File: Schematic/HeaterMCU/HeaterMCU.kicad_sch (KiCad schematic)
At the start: 59 parts, among them J301 To PSU Board, J302 Heater Control, J303 High voltage warning, J304 Firmware, SW301 RESET, U301 Display_IPS_1.3_SPI, U302 ATMEGA328P-AU, U303 TLP185, U304 INA219AIDCNR, U305 TLP185, U306 TPS54302, Y301 8MHz

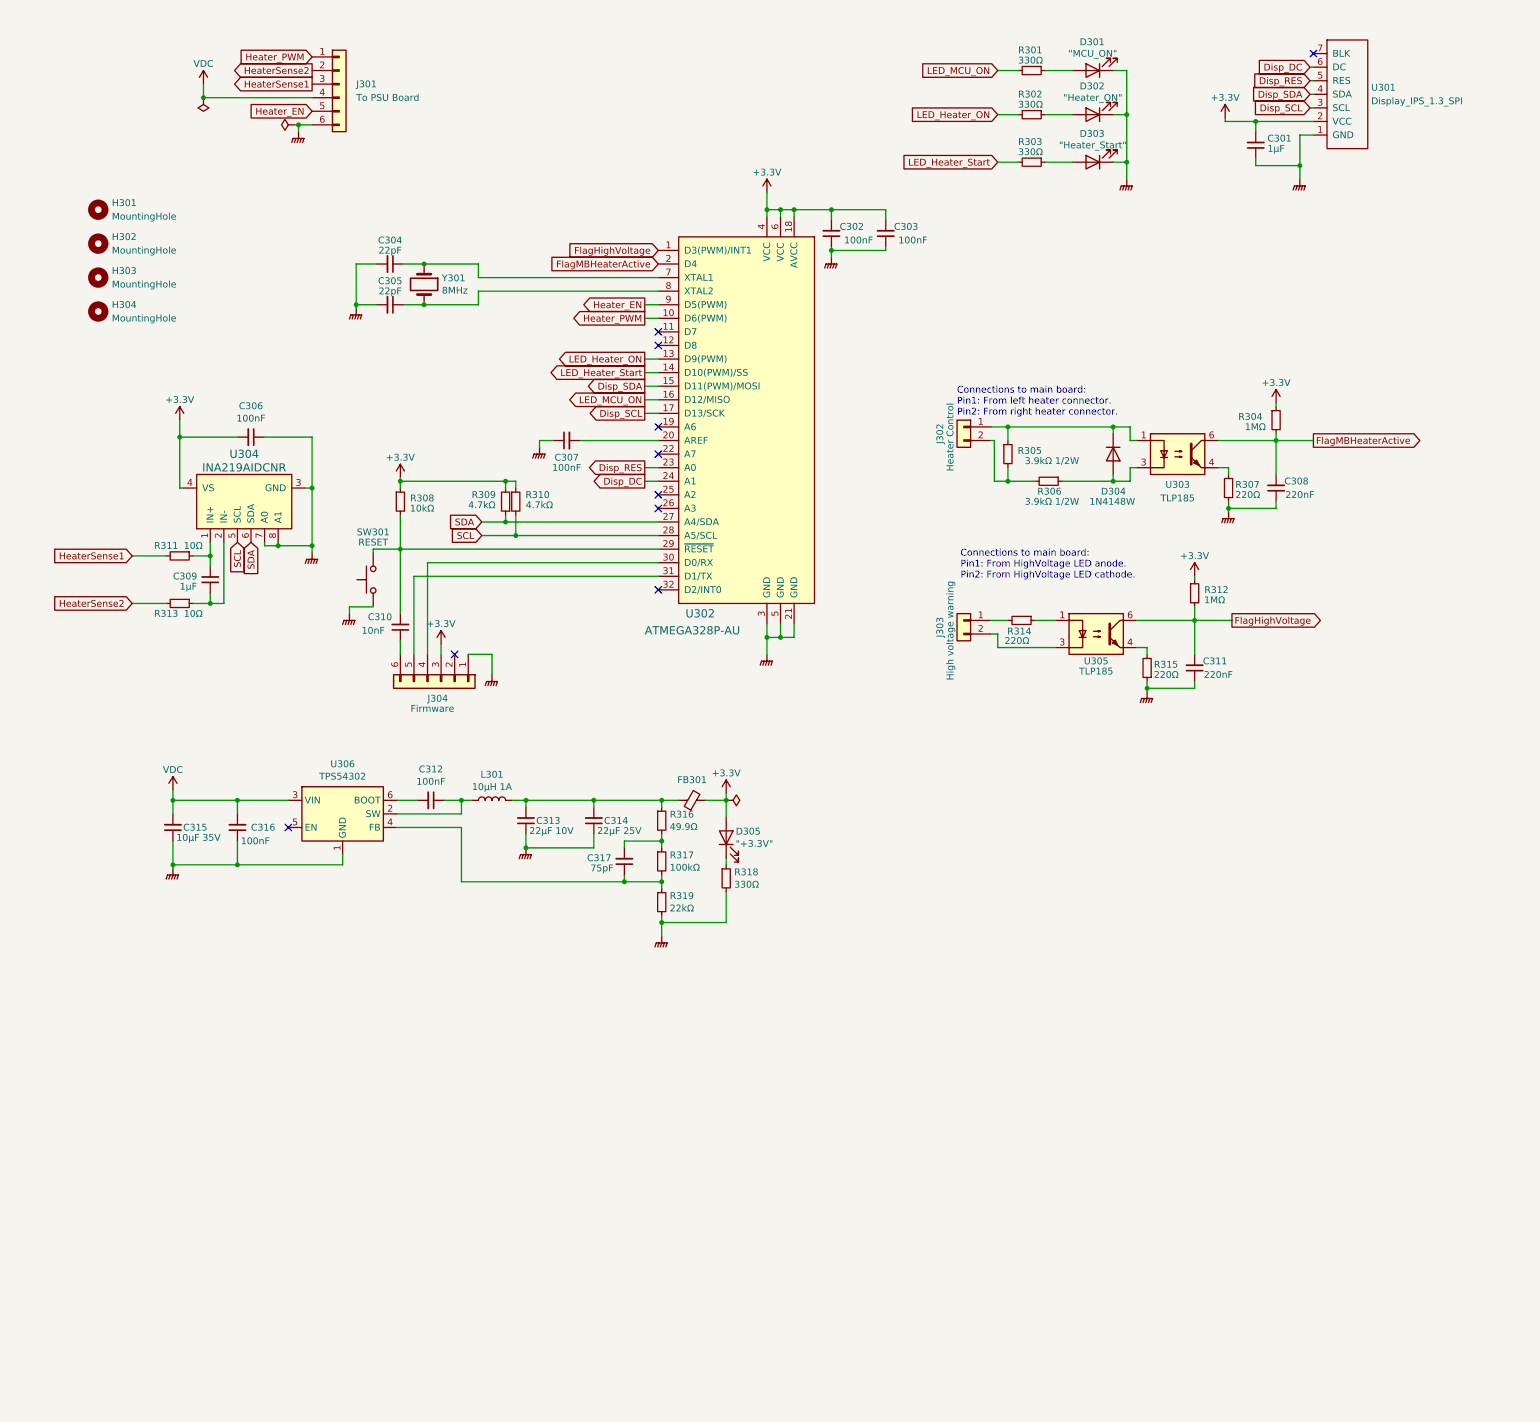
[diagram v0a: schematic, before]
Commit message: New PSU based on XL4005
Added current limiter
Added interface to uTracer PIC
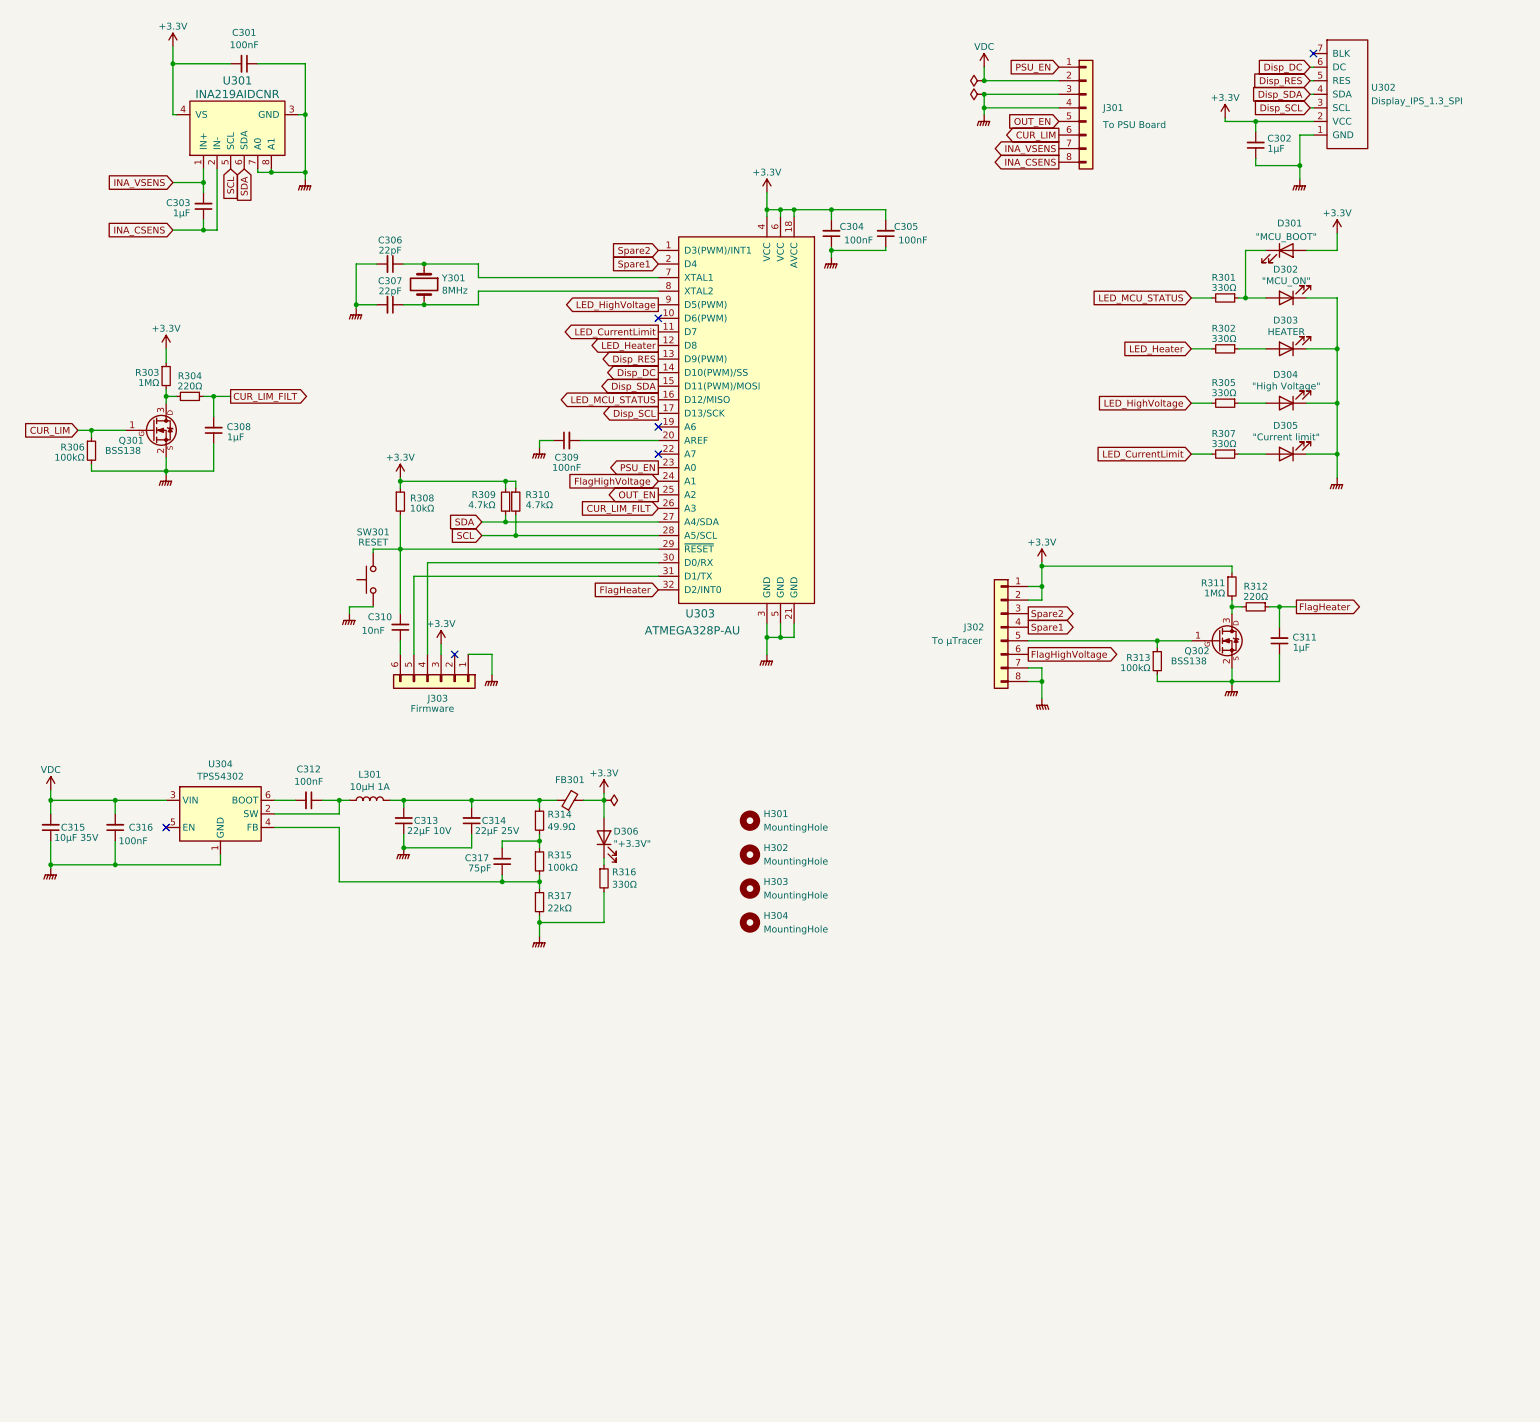
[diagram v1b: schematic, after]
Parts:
- removed D304: 1N4148W, Diode_SMD:D_SOD-123, symbol Diode:1N4148W
- removed J301: To PSU Board, Connector_PinSocket_2.54mm:PinSocket_1x06_P2.54mm_Vertical, symbol Connector_Generic:Conn_01x06
- removed J302: Heater Control, Connector_PinSocket_2.54mm:PinSocket_1x02_P2.54mm_Horizontal, symbol Connector_Generic:Conn_01x02
- removed J303: High voltage warning, Connector_PinSocket_2.54mm:PinSocket_1x02_P2.54mm_Horizontal, symbol Connector_Generic:Conn_01x02
- removed R305: 3.9kΩ 1/2W, Resistor_SMD:R_1210_3225Metric_Pad1.30x2.65mm_HandSolder, symbol Device:R_Small
- removed R314, R315: 220Ω, Resistor_SMD:R_0603_1608Metric_Pad0.98x0.95mm_HandSolder, symbol Device:R_Small
- removed U303, U305: TLP185, Package_SO:SOIC-4_4.55x3.7mm_P2.54mm, symbol Isolator:TLP185
- added D301: "MCU_BOOT", LED_SMD:LED_0603_1608Metric_Pad1.05x0.95mm_HandSolder, symbol Device:LED
- added D305: "Current limit", LED_SMD:LED_0603_1608Metric_Pad1.05x0.95mm_HandSolder, symbol Device:LED
- added J301: To PSU Board, Connector_PinHeader_2.54mm:PinHeader_1x08_P2.54mm_Vertical, symbol Connector_Generic:Conn_01x08
- added J302: To µTracer, myDevices:0527450897, symbol Connector_Generic:Conn_01x08
- added Q301, Q302: BSS138, Package_TO_SOT_SMD:SOT-23, symbol myDevices:BSS138
- added R303: 1MΩ, Resistor_SMD:R_0603_1608Metric_Pad0.98x0.95mm_HandSolder, symbol Device:R_Small
- C308, C311: value 220nF -> 1µF
- D303: renamed from D302; value "Heater_ON" -> HEATER
- D304: renamed from D303; value "Heater_Start" -> "High Voltage"
- R304, R312: value 1MΩ -> 220Ω
- R306: value 3.9kΩ 1/2W -> 100kΩ; footprint Resistor_SMD:R_1210_3225Metric_Pad1.30x2.65mm_HandSolder -> Resistor_SMD:R_0603_1608Metric_Pad0.98x0.95mm_HandSolder
- R307: value 220Ω -> 330Ω
- R311: value 10Ω -> 1MΩ
- R313: value 10Ω -> 100kΩ
- renumbered C306 to C301, C301 to C302, C309 to C303, C302 to C304, C303 to C305, C304 to C306, C305 to C307, C307 to C309, D301 to D302, D305 to D306, J304 to J303, R303 to R305, R316 to R314, R317 to R315, R318 to R316, R319 to R317, U304 to U301, U301 to U302, U302 to U303, U306 to U304
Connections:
- net HeaterSense2 is gone; now on net GNDPWR: R313.2
- net +3V3: now also R311.1, D301.2 (A), J302.1 (Pin_1), J302.2 (Pin_2), R303.1; no longer R304.1, R312.1
- net Disp_DC: now also U303.14 (D10(PWM)/SS); no longer U303.24 (A1)
- net Disp_RES: now also U303.13 (D9(PWM)); no longer U303.23 (A0)
- net FlagHighVoltage: now also U303.24 (A1), J302.6 (Pin_6); no longer C311.2, R312.2, U303.1 (D3(PWM)/INT1)
- net GNDPWR: now also R306.2, D305.1 (K), J301.3 (Pin_3), J301.4 (Pin_4), J302.7 (Pin_7), J302.8 (Pin_8), Q301.2 (S), Q302.2 (S); no longer R307.1
- net VDC: now also J301.2 (Pin_2)
- net INA_CSENS: now reaches C303.1, U301.2 (IN-)
- net INA_CSENS: now also J301.8 (Pin_8); no longer R313.1
- net INA_VSENS: now reaches C303.2, U301.1 (IN+)
- net INA_VSENS: now also J301.7 (Pin_7); no longer R311.1
- net LED_CurrentLimit: now reaches R307.2
- net LED_CurrentLimit: now also U303.11 (D7)
- net CUR_LIM: now reaches R306.1
- net CUR_LIM: now also J301.6 (Pin_6), Q301.1 (G)
- net LED_Heater: now reaches U303.12 (D8)
- net LED_Heater: now also R302.2
- net OUT_EN: now reaches U303.25 (A2)
- net OUT_EN: now also J301.5 (Pin_5)
- net CUR_LIM_FILT: now reaches U303.26 (A3)
- net CUR_LIM_FILT: now also C308.2, R304.1
- net FlagHeater: now reaches U303.32 (D2/INT0)
- net FlagHeater: now also C311.2, R312.1
- net at D302.2 (A), R301.1: now also D301.1 (K)
- removed net FlagMBHeaterActive: C308.2, R304.2, U303.2 (D4)
- net HeaterSense1: no longer names the net of R311.2
- net HeaterSense1: now also R312.2, Q302.3 (D)
- net Heater_EN renamed LED_HighVoltage
- net LED_HighVoltage: now also R305.2
- net Heater_PWM: no longer names the net of U303.10 (D6(PWM))
- removed net LED_Heater_ON: R302.2, U303.13 (D9(PWM))
- removed net LED_Heater_Start: R305.2, U303.14 (D10(PWM)/SS)
- net LED_MCU_ON renamed LED_MCU_STATUS
- new net: Q301.3 (D), R303.2, R304.2
- new net: J302.5 (Pin_5), Q302.1 (G), R313.1
- new net: D305.2 (A), R307.1
- new net PSU_EN: J301.1 (Pin_1), U303.23 (A0)
- new net Spare1: J302.4 (Pin_4), U303.2 (D4)
- new net Spare2: J302.3 (Pin_3), U303.1 (D3(PWM)/INT1)
- no-connect marks 10 -> 6
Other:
- note removed: "Connections to main board: Pin1: From HighVoltage LED anode. Pin2: From HighVoltage LED cathode."
- note removed: "Connections to main board: Pin1: From left heater connector. Pin2: From right heater connector."
- moved on the sheet: C301, C303, C312, C313, C314, C315, C316, C317, D302, D303, D304, D306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

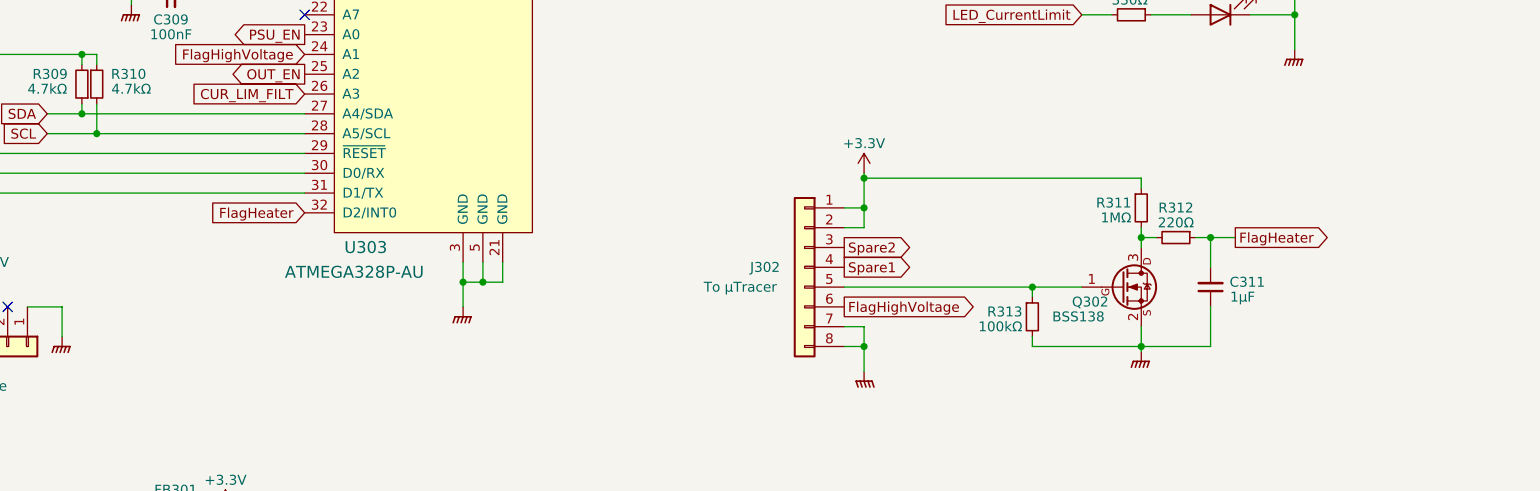
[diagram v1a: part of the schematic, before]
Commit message: PIC interface board, version A
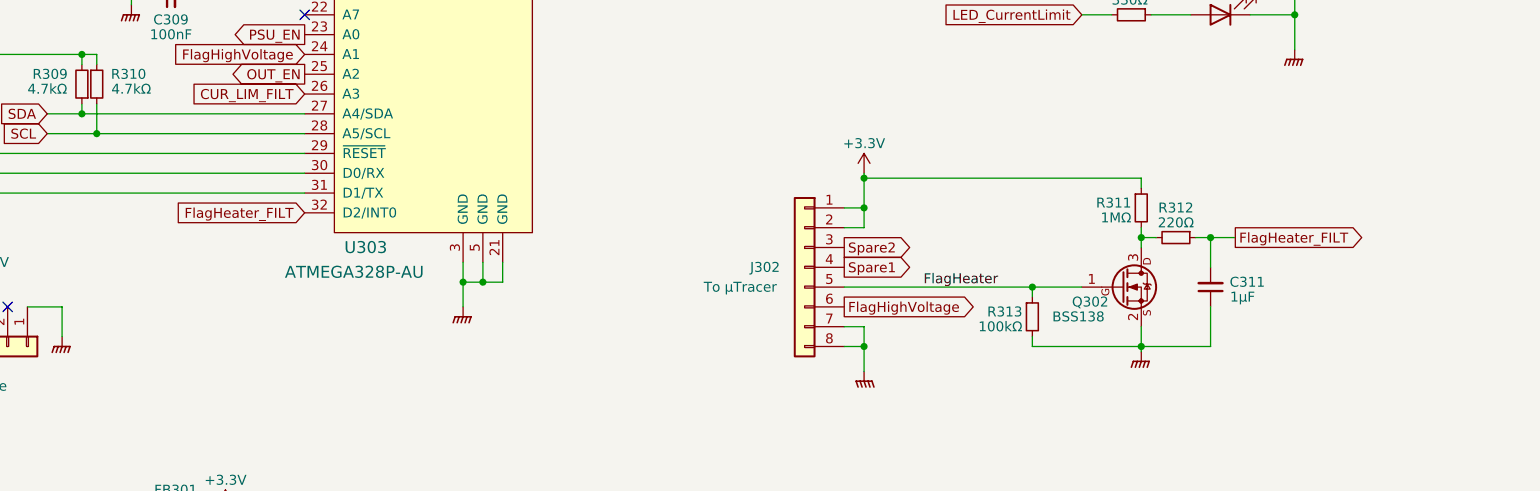
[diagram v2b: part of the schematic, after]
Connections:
- net FlagHeater: now also J302.5 (Pin_5), Q302.1 (G), R313.1; no longer C311.2, R312.1, U303.32 (D2/INT0)
- new net FlagHeater_FILT: C311.2, R312.1, U303.32 (D2/INT0)
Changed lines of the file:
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@@
     (stroke (width 0) (type default) (color 0 0 0 0))
+  )
+  (label "FlagHeater" (at 213.36 130.81 0)
+    (effects (font (size 1.27 1.27)) (justify left bottom))
   )
   (global_label "LED_CurrentLimit" (shape input) (at 233.68 95.885 180) (fields_autoplaced)
@@
     )
   )
-  (global_label "FlagHeater" (shape input) (at 133.985 121.285 180) (fields_autoplaced)
+  (global_label "FlagHeater_FILT" (shape input) (at 133.985 121.285 180) (fields_autoplaced)
     (effects (font (size 1.27 1.27)) (justify right))
-    (property "Intersheet References" "${INTERSHEET_REFS}" (id 0) (at 121.3514 121.2056 0)
+    (property "Intersheet References" "${INTERSHEET_REFS}" (id 0) (at 116.6948 121.2056 0)
       (effects (font (size 1.27 1.27)) (justify right) hide)
     )
@@
     )
   )
-  (global_label "FlagHeater" (shape output) (at 253.365 124.46 0) (fields_autoplaced)
+  (global_label "FlagHeater_FILT" (shape output) (at 253.365 124.46 0) (fields_autoplaced)
     (effects (font (size 1.27 1.27)) (justify left))
-    (property "Intersheet References" "${INTERSHEET_REFS}" (id 0) (at 265.9986 124.3806 0)
+    (property "Intersheet References" "${INTERSHEET_REFS}" (id 0) (at 270.6552 124.3806 0)
       (effects (font (size 1.27 1.27)) (justify left) hide)
     )
